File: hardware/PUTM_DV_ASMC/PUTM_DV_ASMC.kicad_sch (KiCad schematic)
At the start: 0 parts

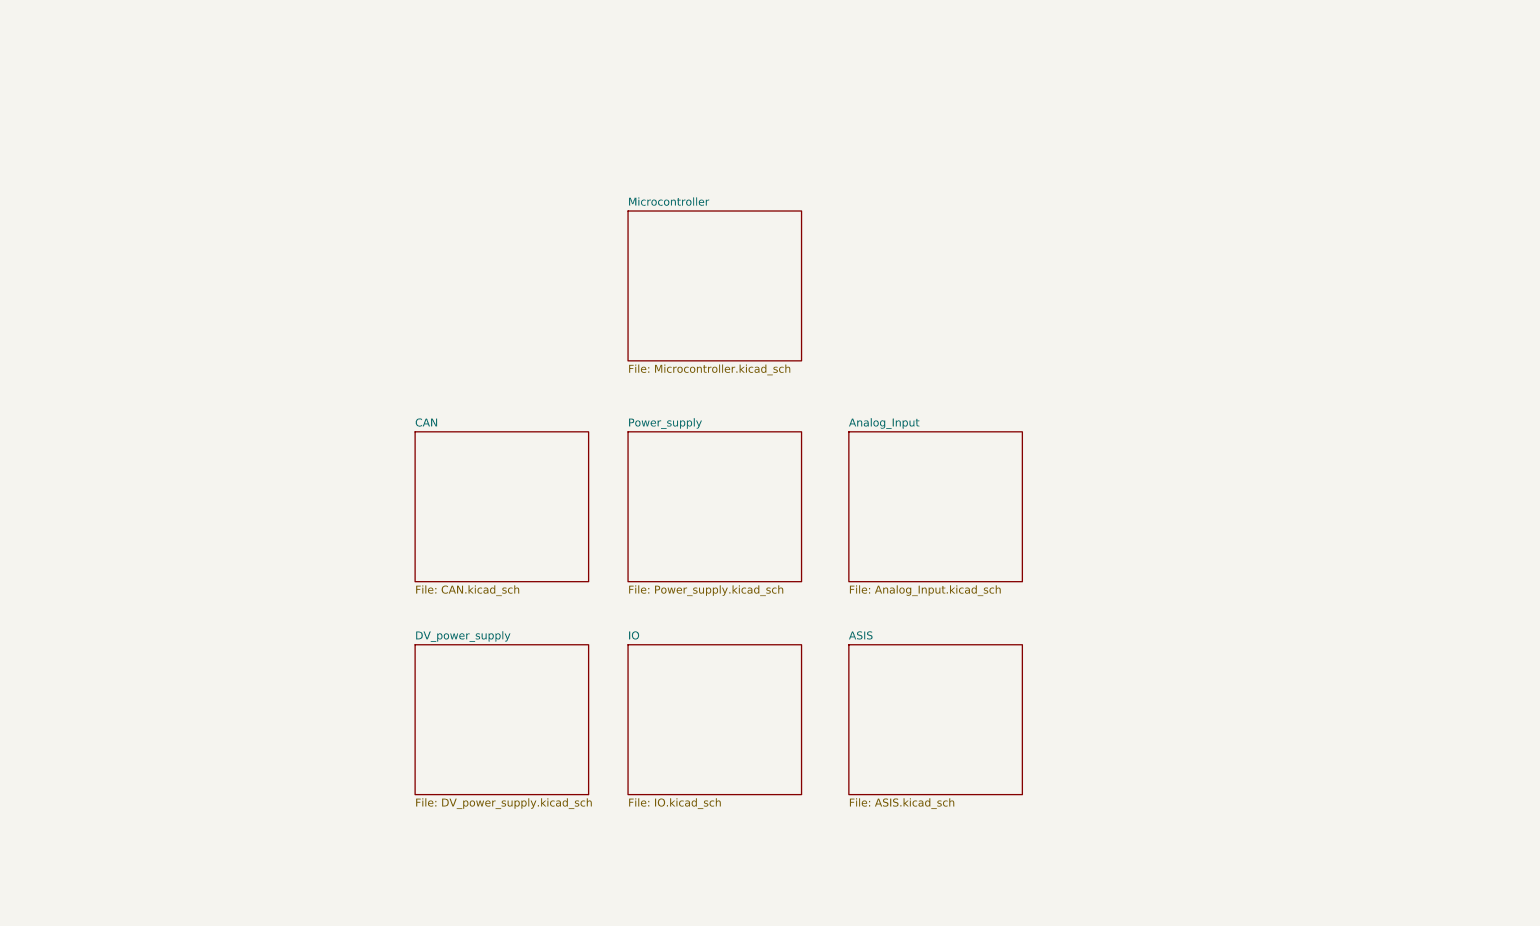
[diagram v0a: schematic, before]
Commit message: schematics without main connector
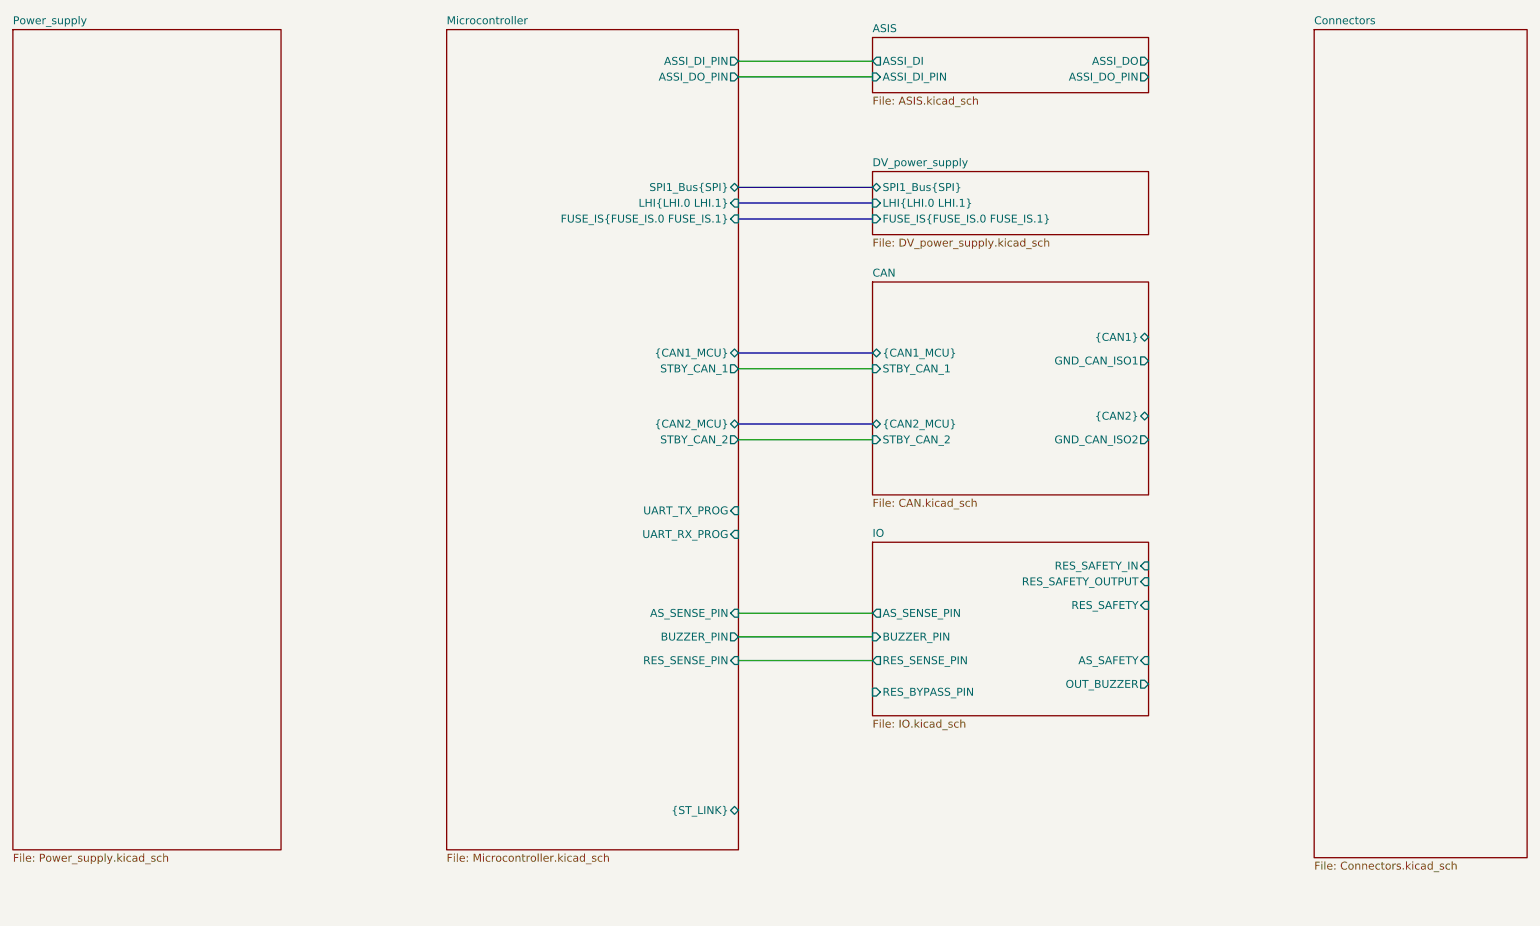
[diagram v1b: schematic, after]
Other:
- removed sheet Analog_Input
- added sheet Connectors (Connectors.kicad_sch)
- sheet ASIS ports: added ASSI_DI, ASSI_DI_PIN, ASSI_DO, ASSI_DO_PIN; removed none
- sheet CAN ports: added GND_CAN_ISO1, GND_CAN_ISO2, STBY_CAN_1, STBY_CAN_2, {CAN1_MCU}, {CAN1}, {CAN2_MCU}, {CAN2}; removed none
- sheet DV_power_supply ports: added FUSE_IS{FUSE_IS.0 FUSE_IS.1}, LHI{LHI.0 LHI.1}, SPI1_Bus{SPI}; removed none
- sheet IO ports: added AS_SAFETY, AS_SENSE_PIN, BUZZER_PIN, OUT_BUZZER, RES_BYPASS_PIN, RES_SAFETY, RES_SAFETY_IN, RES_SAFETY_OUTPUT, RES_SENSE_PIN; removed none
- sheet Microcontroller ports: added ASSI_DI_PIN, ASSI_DO_PIN, AS_SENSE_PIN, BUZZER_PIN, FUSE_IS{FUSE_IS.0 FUSE_IS.1}, LHI{LHI.0 LHI.1}, RES_SENSE_PIN, SPI1_Bus{SPI}, STBY_CAN_1, STBY_CAN_2, UART_RX_PROG, UART_TX_PROG, {CAN1_MCU}, {CAN2_MCU}, {ST_LINK}; removed none

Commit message: done schematic v1
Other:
- sheet Connectors ports: added ADC, ASSI_DI, ASSI_DO, AS_SAFETY, GND_CAN_ISO1, GND_CAN_ISO2, GPIO, OUTPUT_ODRIVE, OUT_ASSI, OUT_BUZZER, OUT_EBS, OUT_LIDAR, OUT_RES, RES_SAFETY, RES_SAFETY_IN, RES_SAFETY_OUTPUT, UART_RX_PROG, UART_TX_PROG, {CAN1}, {CAN2}, {ST-LINK}; removed none
- sheet DV_power_supply ports: added OUT_ASSI, OUT_EBS, OUT_LIDAR, OUT_ODRIVE, OUT_RES; removed none
- sheet Microcontroller ports: added ADC, GPIO, RES_BYPASS_PIN; removed none
- note added: "Isolated"

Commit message: schematic without error
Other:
- sheet Connectors ports: added ODRIVE[1..4]; removed OUTPUT_ODRIVE
- sheet DV_power_supply ports: added FUSE_ISO{FUSE_ISO.0 FUSE_ISO.1}, ODRIVE[1..4]; removed FUSE_IS{FUSE_IS.0 FUSE_IS.1}, OUT_ODRIVE
- sheet Microcontroller ports: added FUSE_ISO{FUSE_ISO.0 FUSE_ISO.1}; removed FUSE_IS{FUSE_IS.0 FUSE_IS.1}
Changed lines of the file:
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@@
-	(wire
-		(pts
-			(xy 210.82 58.42) (xy 237.49 58.42)
-		)
-		(stroke
-			(width 0)
-			(type default)
-		)
-	)
 	(wire
 		(pts
@@
 		(pts
 			(xy 210.82 120.65) (xy 237.49 120.65)
+		)
+		(stroke
+			(width 0)
+			(type default)
+		)
+	)
+	(bus
+		(pts
+			(xy 210.82 60.96) (xy 237.49 60.96)
 		)
 		(stroke
@@
 			)
 		)
-		(pin "OUTPUT_ODRIVE" input
-			(at 237.49 58.42 180)
-			(effects
-				(font
-					(size 1.27 1.27)
-				)
-				(justify left)
-			)
-		)
 		(pin "OUT_ASSI" input
 			(at 237.49 43.18 180)
@@
 		(pin "GPIO" bidirectional
 			(at 237.49 111.76 180)
+			(effects
+				(font
+					(size 1.27 1.27)
+				)
+				(justify left)
+			)
+		)
+		(pin "ODRIVE[1..4]" input
+			(at 237.49 60.96 180)
 			(effects
 				(font
@@
 			)
 		)
-		(pin "FUSE_IS{FUSE_IS.0 FUSE_IS.1}" input
-			(at 166.37 57.15 180)
-			(effects
-				(font
-					(size 1.27 1.27)
-				)
-				(justify left)
-			)
-		)
 		(pin "LHI{LHI.0 LHI.1}" input
 			(at 166.37 50.8 180)
@@
 			)
 		)
-		(pin "OUT_ODRIVE" output
-			(at 210.82 58.42 0)
-			(effects
-				(font
-					(size 1.27 1.27)
-				)
-				(justify right)
-			)
-		)
 		(pin "OUT_RES" output
 			(at 210.82 46.99 0)
+			(effects
+				(font
+					(size 1.27 1.27)
+				)
+				(justify right)
+			)
+		)
+		(pin "FUSE_ISO{FUSE_ISO.0 FUSE_ISO.1}" output
+			(at 166.37 57.15 180)
+			(effects
+				(font
+					(size 1.27 1.27)
+				)
+				(justify left)
+			)
+		)
+		(pin "ODRIVE[1..4]" output
+			(at 210.82 60.96 0)
 			(effects
 				(font
@@
 			)
 		)
-		(pin "FUSE_IS{FUSE_IS.0 FUSE_IS.1}" input
-			(at 144.78 57.15 0)
-			(effects
-				(font
-					(size 1.27 1.27)
-				)
-				(justify right)
-			)
-		)
 		(pin "LHI{LHI.0 LHI.1}" input
 			(at 144.78 50.8 0)
@@
 			(effects
 				(font
+					(size 1.27 1.27)
+				)
+				(justify right)
+			)
+		)
+		(pin "FUSE_ISO{FUSE_ISO.0 FUSE_ISO.1}" input
+			(at 144.78 57.15 0)
+			(effects
+				(font

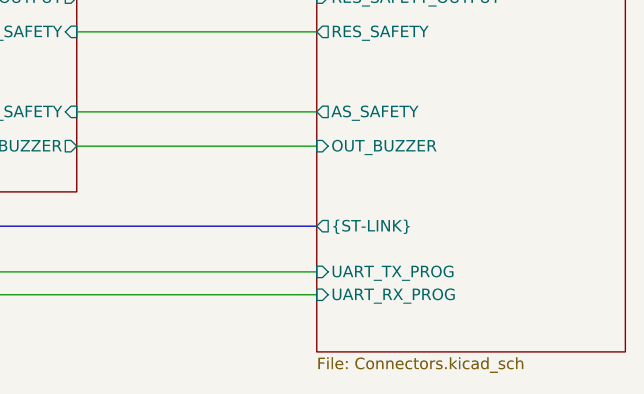
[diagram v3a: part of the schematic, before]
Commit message: tylko dwa bledy z can - schemat na wykonczeniu
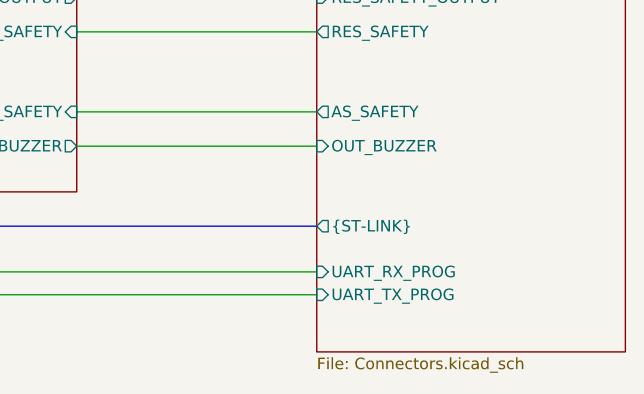
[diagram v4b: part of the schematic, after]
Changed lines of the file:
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@@
+	(wire
+		(pts
+			(xy 210.82 54.61) (xy 237.49 54.61)
+		)
+		(stroke
+			(width 0)
+			(type default)
+		)
+	)
+	(wire
+		(pts
+			(xy 210.82 50.8) (xy 237.49 50.8)
+		)
+		(stroke
+			(width 0)
+			(type default)
+		)
+	)
+	(wire
+		(pts
+			(xy 144.78 109.22) (xy 237.49 109.22)
+		)
+		(stroke
+			(width 0)
+			(type default)
+		)
+	)
+	(wire
+		(pts
+			(xy 144.78 83.82) (xy 166.37 83.82)
+		)
+		(stroke
+			(width 0)
+			(type default)
+		)
+	)
+	(wire
+		(pts
+			(xy 144.78 135.89) (xy 166.37 135.89)
+		)
+		(stroke
+			(width 0)
+			(type default)
+		)
+	)
+	(bus
+		(pts
+			(xy 210.82 78.74) (xy 237.49 78.74)
+		)
+		(stroke
+			(width 0)
+			(type default)
+		)
+	)
+	(wire
+		(pts
+			(xy 144.78 156.21) (xy 237.49 156.21)
+		)
+		(stroke
+			(width 0)
+			(type default)
+		)
+	)
+	(wire
+		(pts
+			(xy 210.82 120.65) (xy 237.49 120.65)
+		)
+		(stroke
+			(width 0)
+			(type default)
+		)
+	)
+	(bus
+		(pts
+			(xy 210.82 60.96) (xy 237.49 60.96)
+		)
+		(stroke
+			(width 0)
+			(type default)
+		)
+	)
+	(wire
+		(pts
+			(xy 144.78 30.48) (xy 166.37 30.48)
+		)
+		(stroke
+			(width 0)
+			(type default)
+		)
+	)
+	(wire
+		(pts
+			(xy 144.78 95.25) (xy 166.37 95.25)
+		)
+		(stroke
+			(width 0)
+			(type default)
+		)
+	)
+	(bus
+		(pts
+			(xy 144.78 81.28) (xy 166.37 81.28)
+		)
+		(stroke
+			(width 0)
+			(type default)
+		)
+	)
+	(bus
+		(pts
+			(xy 144.78 57.15) (xy 166.37 57.15)
+		)
+		(stroke
+			(width 0)
+			(type default)
+		)
+	)
 	(wire
 		(pts
@@
 	(wire
 		(pts
-			(xy 210.82 54.61) (xy 237.49 54.61)
-		)
-		(stroke
-			(width 0)
-			(type default)
-		)
-	)
-	(wire
-		(pts
-			(xy 210.82 50.8) (xy 237.49 50.8)
-		)
-		(stroke
-			(width 0)
-			(type default)
-		)
-	)
-	(wire
-		(pts
-			(xy 144.78 109.22) (xy 237.49 109.22)
-		)
-		(stroke
-			(width 0)
-			(type default)
-		)
-	)
-	(wire
-		(pts
-			(xy 144.78 83.82) (xy 166.37 83.82)
-		)
-		(stroke
-			(width 0)
-			(type default)
-		)
-	)
-	(wire
-		(pts
-			(xy 144.78 135.89) (xy 166.37 135.89)
-		)
-		(stroke
-			(width 0)
-			(type default)
-		)
-	)
-	(bus
-		(pts
-			(xy 210.82 78.74) (xy 237.49 78.74)
-		)
-		(stroke
-			(width 0)
-			(type default)
-		)
-	)
-	(wire
-		(pts
-			(xy 210.82 120.65) (xy 237.49 120.65)
-		)
-		(stroke
-			(width 0)
-			(type default)
-		)
-	)
-	(bus
-		(pts
-			(xy 210.82 60.96) (xy 237.49 60.96)
-		)
-		(stroke
-			(width 0)
-			(type default)
-		)
-	)
-	(wire
-		(pts
-			(xy 144.78 30.48) (xy 166.37 30.48)
-		)
-		(stroke
-			(width 0)
-			(type default)
-		)
-	)
-	(wire
-		(pts
-			(xy 144.78 95.25) (xy 166.37 95.25)
-		)
-		(stroke
-			(width 0)
-			(type default)
-		)
-	)
-	(bus
-		(pts
-			(xy 144.78 81.28) (xy 166.37 81.28)
-		)
-		(stroke
-			(width 0)
-			(type default)
-		)
-	)
-	(bus
-		(pts
-			(xy 144.78 57.15) (xy 166.37 57.15)
-		)
-		(stroke
-			(width 0)
-			(type default)
-		)
-	)
-	(wire
-		(pts
 			(xy 210.82 46.99) (xy 237.49 46.99)
 		)
@@
 		(pts
 			(xy 210.82 82.55) (xy 237.49 82.55)
-		)
-		(stroke
-			(width 0)
-			(type default)
-		)
-	)
-	(wire
-		(pts
-			(xy 144.78 156.21) (xy 237.49 156.21)
 		)
 		(stroke
@@
 		)
 		(pin "UART_RX_PROG" input
+			(at 237.49 153.67 180)
+			(effects
+				(font
+					(size 1.27 1.27)
+				)
+				(justify left)
+			)
+		)
+		(pin "UART_TX_PROG" input
 			(at 237.49 156.21 180)
 			(effects
 				(font
-					(size 1.27 1.27)
-				)
-				(justify left)
-			)
-		)
-		(pin "UART_TX_PROG" input
-			(at 237.49 153.67 180)
-			(effects
-				(font

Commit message: work on supply and zones
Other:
- sheet DV_power_supply ports: added FUSE_IS[0..1], LHI[0..1], SPI1{NSS SCK MISO MOSI}; removed FUSE_ISO{FUSE_ISO.0 FUSE_ISO.1}, LHI{LHI.0 LHI.1}, SPI1_Bus{SPI}
- sheet Microcontroller ports: added FUSE_IS[0..1], LHI[0..1], SPI1{NSS SCK MISO MOSI}; removed FUSE_ISO{FUSE_ISO.0 FUSE_ISO.1}, LHI{LHI.0 LHI.1}, SPI1_Bus{SPI}
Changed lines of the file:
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@@
-			)
-		)
-		(pin "LHI{LHI.0 LHI.1}" input
-			(at 166.37 50.8 180)
-			(effects
-				(font
-					(size 1.27 1.27)
-				)
-				(justify left)
-			)
-		)
-		(pin "SPI1_Bus{SPI}" bidirectional
-			(at 166.37 44.45 180)
-			(effects
-				(font
-					(size 1.27 1.27)
-				)
-				(justify left)
 			)
 		)
@@
 			)
 		)
-		(pin "FUSE_ISO{FUSE_ISO.0 FUSE_ISO.1}" output
-			(at 166.37 57.15 180)
-			(effects
-				(font
-					(size 1.27 1.27)
-				)
-				(justify left)
-			)
-		)
 		(pin "ODRIVE[1..4]" output
 			(at 210.82 60.96 0)
@@
 				)
 				(justify right)
+			)
+		)
+		(pin "SPI1{NSS SCK MISO MOSI}" bidirectional
+			(at 166.37 44.45 180)
+			(effects
+				(font
+					(size 1.27 1.27)
+				)
+				(justify left)
+			)
+		)
+		(pin "FUSE_IS[0..1]" output
+			(at 166.37 57.15 180)
+			(effects
+				(font
+					(size 1.27 1.27)
+				)
+				(justify left)
+			)
+		)
+		(pin "LHI[0..1]" input
+			(at 166.37 50.8 180)
+			(effects
+				(font
+					(size 1.27 1.27)
+				)
+				(justify left)
 			)
 		)
@@
 			)
 		)
-		(pin "LHI{LHI.0 LHI.1}" input
-			(at 144.78 50.8 0)
-			(effects
-				(font
-					(size 1.27 1.27)
-				)
-				(justify right)
-			)
-		)
 		(pin "RES_SENSE_PIN" input
 			(at 144.78 135.89 0)
@@
 			)
 		)
-		(pin "SPI1_Bus{SPI}" bidirectional
-			(at 144.78 44.45 0)
-			(effects
-				(font
-					(size 1.27 1.27)
-				)
-				(justify right)
-			)
-		)
 		(pin "STBY_CAN_1" output
 			(at 144.78 83.82 0)
@@
 			)
 		)
-		(pin "FUSE_ISO{FUSE_ISO.0 FUSE_ISO.1}" input
+		(pin "SPI1{NSS SCK MISO MOSI}" bidirectional
+			(at 144.78 44.45 0)
+			(effects
+				(font
+					(size 1.27 1.27)
+				)
+				(justify right)
+			)
+		)
+		(pin "FUSE_IS[0..1]" input
 			(at 144.78 57.15 0)
 			(effects
 				(font
+					(size 1.27 1.27)
+				)
+				(justify right)
+			)
+		)
+		(pin "LHI[0..1]" input
+			(at 144.78 50.8 0)
+			(effects
+				(font

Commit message: work work work
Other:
- sheet Microcontroller ports: added {ST-LINK}; removed {ST_LINK}
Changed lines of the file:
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@@
+			)
+		)
+		(pin "{CAN2}" bidirectional
+			(at 210.82 91.44 0)
+			(effects
+				(font
+					(size 1.27 1.27)
+				)
+				(justify right)
 			)
 		)
@@
 			)
 		)
+		(pin "{CAN2_MCU}" bidirectional
+			(at 166.37 92.71 180)
+			(effects
+				(font
+					(size 1.27 1.27)
+				)
+				(justify left)
+			)
+		)
 		(pin "{CAN1}" bidirectional
 			(at 210.82 78.74 0)
-			(effects
-				(font
-					(size 1.27 1.27)
-				)
-				(justify right)
-			)
-		)
-		(pin "{CAN2_MCU}" bidirectional
-			(at 166.37 92.71 180)
-			(effects
-				(font
-					(size 1.27 1.27)
-				)
-				(justify left)
-			)
-		)
-		(pin "{CAN2}" bidirectional
-			(at 210.82 91.44 0)
 			(effects
 				(font
@@
 			)
 		)
+		(pin "{CAN2}" bidirectional
+			(at 237.49 91.44 180)
+			(effects
+				(font
+					(size 1.27 1.27)
+				)
+				(justify left)
+			)
+		)
+		(pin "{ST-LINK}" output
+			(at 237.49 148.59 180)
+			(effects
+				(font
+					(size 1.27 1.27)
+				)
+				(justify left)
+			)
+		)
+		(pin "ADC" bidirectional
+			(at 237.49 109.22 180)
+			(effects
+				(font
+					(size 1.27 1.27)
+				)
+				(justify left)
+			)
+		)
+		(pin "GPIO" bidirectional
+			(at 237.49 111.76 180)
+			(effects
+				(font
+					(size 1.27 1.27)
+				)
+				(justify left)
+			)
+		)
+		(pin "ODRIVE[1..4]" input
+			(at 237.49 60.96 180)
+			(effects
+				(font
+					(size 1.27 1.27)
+				)
+				(justify left)
+			)
+		)
 		(pin "{CAN1}" bidirectional
 			(at 237.49 78.74 180)
-			(effects
-				(font
-					(size 1.27 1.27)
-				)
-				(justify left)
-			)
-		)
-		(pin "{CAN2}" bidirectional
-			(at 237.49 91.44 180)
-			(effects
-				(font
-					(size 1.27 1.27)
-				)
-				(justify left)
-			)
-		)
-		(pin "{ST-LINK}" output
-			(at 237.49 148.59 180)
-			(effects
-				(font
-					(size 1.27 1.27)
-				)
-				(justify left)
-			)
-		)
-		(pin "ADC" bidirectional
-			(at 237.49 109.22 180)
-			(effects
-				(font
-					(size 1.27 1.27)
-				)
-				(justify left)
-			)
-		)
-		(pin "GPIO" bidirectional
-			(at 237.49 111.76 180)
-			(effects
-				(font
-					(size 1.27 1.27)
-				)
-				(justify left)
-			)
-		)
-		(pin "ODRIVE[1..4]" input
-			(at 237.49 60.96 180)
 			(effects
 				(font
@@
 			)
 		)
+		(pin "{ST-LINK}" input
+			(at 144.78 148.59 0)
+			(effects
+				(font
+					(size 1.27 1.27)
+				)
+				(justify right)
+			)
+		)
+		(pin "BUZZER_PIN" output
+			(at 144.78 132.08 0)
+			(effects
+				(font
+					(size 1.27 1.27)
+				)
+				(justify right)
+			)
+		)
+		(pin "UART_RX_PROG" input
+			(at 144.78 153.67 0)
+			(effects
+				(font
+					(size 1.27 1.27)
+				)
+				(justify right)
+			)
+		)
+		(pin "UART_TX_PROG" input
+			(at 144.78 156.21 0)
+			(effects
+				(font
+					(size 1.27 1.27)
+				)
+				(justify right)
+			)
+		)
+		(pin "ADC" bidirectional
+			(at 144.78 109.22 0)
+			(effects
+				(font
+					(size 1.27 1.27)
+				)
+				(justify right)
+			)
+		)
+		(pin "GPIO" bidirectional
+			(at 144.78 111.76 0)
+			(effects
+				(font
+					(size 1.27 1.27)
+				)
+				(justify right)
+			)
+		)
+		(pin "RES_BYPASS_PIN" output
+			(at 144.78 140.97 0)
+			(effects
+				(font
+					(size 1.27 1.27)
+				)
+				(justify right)
+			)
+		)
+		(pin "SPI1{NSS SCK MISO MOSI}" bidirectional
+			(at 144.78 44.45 0)
+			(effects
+				(font
+					(size 1.27 1.27)
+				)
+				(justify right)
+			)
+		)
+		(pin "FUSE_IS[0..1]" input
+			(at 144.78 57.15 0)
+			(effects
+				(font
+					(size 1.27 1.27)
+				)
+				(justify right)
+			)
+		)
+		(pin "LHI[0..1]" input
+			(at 144.78 50.8 0)
+			(effects
+				(font
+					(size 1.27 1.27)
+				)
+				(justify right)
+			)
+		)
 		(pin "{CAN1_MCU}" bidirectional
 			(at 144.78 81.28 0)
@@
 			(effects
 				(font
-					(size 1.27 1.27)
-				)
-				(justify right)
-			)
-		)
-		(pin "{ST_LINK}" bidirectional
-			(at 144.78 148.59 0)
-			(effects
-				(font
-					(size 1.27 1.27)
-				)
-				(justify right)
-			)
-		)
-		(pin "BUZZER_PIN" output
-			(at 144.78 132.08 0)
-			(effects
-				(font
-					(size 1.27 1.27)
-				)
-				(justify right)
-			)
-		)
-		(pin "UART_RX_PROG" input
-			(at 144.78 153.67 0)
-			(effects
-				(font
-					(size 1.27 1.27)
-				)
-				(justify right)
-			)
-		)
-		(pin "UART_TX_PROG" input
-			(at 144.78 156.21 0)
-			(effects
-				(font
-					(size 1.27 1.27)
-				)
-				(justify right)
-			)
-		)
-		(pin "ADC" bidirectional
-			(at 144.78 109.22 0)
-			(effects
-				(font
-					(size 1.27 1.27)
-				)
-				(justify right)
-			)
-		)
-		(pin "GPIO" bidirectional
-			(at 144.78 111.76 0)
-			(effects
-				(font
-					(size 1.27 1.27)
-				)
-				(justify right)
-			)
-		)
-		(pin "RES_BYPASS_PIN" output
-			(at 144.78 140.97 0)
-			(effects
-				(font
-					(size 1.27 1.27)
-				)
-				(justify right)
-			)
-		)
-		(pin "SPI1{NSS SCK MISO MOSI}" bidirectional
-			(at 144.78 44.45 0)
-			(effects
-				(font
-					(size 1.27 1.27)
-				)
-				(justify right)
-			)
-		)
-		(pin "FUSE_IS[0..1]" input
-			(at 144.78 57.15 0)
-			(effects
-				(font
-					(size 1.27 1.27)
-				)
-				(justify right)
-			)
-		)
-		(pin "LHI[0..1]" input
-			(at 144.78 50.8 0)
-			(effects
-				(font
